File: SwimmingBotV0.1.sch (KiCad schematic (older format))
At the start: 15 parts, among them P1 DCMI, P2 ANALOG

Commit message: woohoo getting there
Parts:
- removed W3: GND, Measurement_Points:Measurement_Point_Round-SMD-Pad_Small, symbol TEST_1P
- removed W6: VBAT, Measurement_Points:Measurement_Point_Round-SMD-Pad_Small, symbol TEST_1P
- removed W7: AUX_3.3V, Measurement_Points:Measurement_Point_Round-SMD-Pad_Small, symbol TEST_1P
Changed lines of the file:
@@
 Text Label 7650 1800 2    60   ~ 0
 MOT2_CS#
-Text Label 4400 6200 2    60   ~ 0
+Text Label 4400 6900 2    60   ~ 0
 MOT2_CS#
-Text Label 4400 6100 2    60   ~ 0
+Text Label 4400 7100 2    60   ~ 0
 MOT1_CS#
-Text Label 6550 5850 0    60   ~ 0
+Text Label 4400 7400 2    60   ~ 0
 RF_CRESP#
 Text Label 9900 1800 2    60   ~ 0
@@
 Text Label 9900 1650 2    60   ~ 0
 RF_CRESP#
-Text Label 6550 5950 0    60   ~ 0
+Text Label 4400 7500 2    60   ~ 0
 RF_EX
-Text Label 6550 6050 0    60   ~ 0
+Text Label 6550 6500 0    60   ~ 0
 RF_CMD#
-Text Label 6550 6150 0    60   ~ 0
+Text Label 6550 6600 0    60   ~ 0
 RF_PWR_DWN#
 Text Label 9450 4950 2    60   ~ 0
@@
 Text Label 6550 6350 0    60   ~ 0
 GYRO_FSYNC
-Text Label 6550 6250 0    60   ~ 0
+Text Label 4400 6100 2    60   ~ 0
 GYRO_INT
 Text Label 7650 1400 2    60   ~ 0
@@
 Text Label 3600 1000 0    60   ~ 0
 3.3V_EN
-Text Label 4400 6850 2    60   ~ 0
+Text Label 6550 6800 0    60   ~ 0
 3.3V_EN
 NoConn ~ 4400 5700
@@
 Text Label 7650 2100 2    60   ~ 0
 MOT2_RST#
-Text Label 4400 6300 2    60   ~ 0
+Text Label 6550 5850 0    60   ~ 0
 MOT1_RST#
-Text Label 4400 6400 2    60   ~ 0
+Text Label 6550 6050 0    60   ~ 0
 MOT2_RST#
 Text Label 2700 3300 0    60   ~ 0
@@
 Text Label 1750 2200 0    60   ~ 0
 CHG_EN#
-Text Label 4400 7000 2    60   ~ 0
+Text Label 4400 7300 2    60   ~ 0
 CHG_STAT1
-Text Label 4400 7100 2    60   ~ 0
+Text Label 6550 6700 0    60   ~ 0
 CHG_STAT2
+Text Label 6550 6150 0    60   ~ 0
+CHG_TE#
 Text Label 4400 7200 2    60   ~ 0
-CHG_TE#
-Text Label 4400 7300 2    60   ~ 0
 CHG_EN#
 Text Label 9450 5350 2    60   ~ 0
@@
 Text Label 9450 5650 2    60   ~ 0
 SD_DETECT
-Text Label 6550 6500 0    60   ~ 0
+Text Label 4400 6400 2    60   ~ 0
 SD_CD
-Text Label 6550 6600 0    60   ~ 0
+Text Label 4400 6500 2    60   ~ 0
 SD_DETECT
 Text Label 1750 1100 0    60   ~ 0
 2S_EN
-Text Label 4400 7400 2    60   ~ 0
+Text Label 6550 6250 0    60   ~ 0
 2S_EN
 $Sheet
@@
 F101 "PC10" I R 6550 6150 60
 F102 "PC12" I R 6550 6250 60
-F103 "PD3" I L 4400 6850 60
-F104 "PG11" I R 6550 6700 60
-F105 "PG12" I R 6550 6800 60
-F106 "PG13" I R 6550 6900 60
-F107 "PG14" I R 6550 7000 60
-F108 "PB7" I L 4400 7100 60
-F109 "PB0" I L 4400 7000 60
-F110 "A0" I R 6550 7150 60
-F111 "A1" I R 6550 7250 60
-F112 "A2" I R 6550 7350 60
-F113 "A3" I R 6550 7450 60
+F103 "PG11" I R 6550 6700 60
+F104 "PG12" I R 6550 6800 60
+F105 "PG13" I R 6550 6900 60
+F106 "PG14" I R 6550 7000 60
+F107 "PB0" I L 4400 6900 60
+F108 "A0" I R 6550 7150 60
+F109 "A1" I R 6550 7250 60
+F110 "A2" I R 6550 7350 60
+F111 "A3" I R 6550 7450 60
+F112 "PB11" I L 4400 7000 60
+F113 "PB10" I L 4400 7100 60
 $EndSheet
 $Comp
@@
 Text Label 7100 1250 0    60   ~ 0
 GND
-Text Label 6550 6700 0    60   ~ 0
+Text Label 4400 6200 2    60   ~ 0
 EXT1
-Text Label 6550 6800 0    60   ~ 0
+Text Label 4400 6300 2    60   ~ 0
 EXT2
 Text Label 7450 5150 2    60   ~ 0
@@
 Text Label 7750 5150 2    60   ~ 0
 EXT2
-Text Label 8300 6050 0    60   ~ 0
-GEN_3.3V
 Text Label 8850 1400 0    60   ~ 0
 MOT1_DIAG
 Text Label 8850 1500 0    60   ~ 0
 MOT2_DIAG
-Text Label 4400 6500 2    60   ~ 0
+Text Label 4400 7000 2    60   ~ 0
 MOT1_DIAG
-Text Label 4400 7500 2    60   ~ 0
+Text Label 6550 5950 0    60   ~ 0
 MOT2_DIAG
 Text Label 1750 1700 0    60   ~ 0
@@
 Text Label 6550 7000 0    60   ~ 0
 5V_CHG
-Text Label 8300 5750 0    60   ~ 0
-VBAT
 Text Label 8300 5400 0    60   ~ 0
 SDA
@@
 $EndComp
 $Comp
-L TEST_1P W6
-U 1 1 575A4CA1
-P 8300 5750
-F 0 "W6" H 8300 6020 50  0000 C CNN
-F 1 "VBAT" H 8300 5950 50  0000 C CNN
-F 2 "Measurement_Points:Measurement_Point_Round-SMD-Pad_Small" H 8500 5750 50  0001 C CNN
-F 3 "" H 8500 5750 50  0000 C CNN
-	1    8300 5750
-	0    -1   -1   0
-$EndComp
-$Comp
-L TEST_1P W7
-U 1 1 575A520C
-P 8300 6050
-F 0 "W7" H 8300 6320 50  0000 C CNN
-F 1 "AUX_3.3V" H 8300 6250 50  0000 C CNN
-F 2 "Measurement_Points:Measurement_Point_Round-SMD-Pad_Small" H 8500 6050 50  0001 C CNN
-F 3 "" H 8500 6050 50  0000 C CNN
-	1    8300 6050
-	0    -1   -1   0
-$EndComp
-$Comp
 L LED D4
 U 1 1 575B30FD
@@
 Wire Wire Line
 	7750 4850 7750 4800
-Text Label 8300 6350 0    60   ~ 0
-GND
 Wire Wire Line
 	6600 7250 6550 7250
@@
 Text Label 2600 1050 2    60   ~ 0
 GEN_3.3V
-$Comp
-L TEST_1P W3
-U 1 1 57400D21
-P 8300 6350
-F 0 "W3" H 8300 6620 50  0000 C CNN
-F 1 "GND" H 8300 6550 50  0000 C CNN
-F 2 "Measurement_Points:Measurement_Point_Round-SMD-Pad_Small" H 8500 6350 50  0001 C CNN
-F 3 "" H 8500 6350 50  0000 C CNN
-	1    8300 6350
-	0    -1   -1   0
-$EndComp
 Text Label 6600 7550 0    60   ~ 0
 GND

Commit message: not final, moving towards board v0.2
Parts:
- R19: value 10k -> 4.1k-3.9k
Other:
- note added: "Note: PC13 is limited to an \ninput or v. weak output"
- note added: "gives 2.5v (vref) when\nvbat is 8.6 or so"
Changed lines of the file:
@@
 P 7700 3950
 F 0 "R19" V 7780 3950 50  0000 C CNN
-F 1 "10k" V 7700 3950 50  0000 C CNN
+F 1 "4.1k-3.9k" V 7700 3950 50  0000 C CNN
 F 2 "Resistors_SMD:R_0402" V 7630 3950 50  0001 C CNN
 F 3 "" H 7700 3950 50  0000 C CNN
@@
 	0    -1   -1   0
 $EndComp
+Text Notes 7150 6300 0    60   ~ 0
+Note: PC13 is limited to an \ninput or v. weak output
+Text Notes 8000 3900 0    60   ~ 0
+gives 2.5v (vref) when\nvbat is 8.6 or so
 $EndSCHEMATC

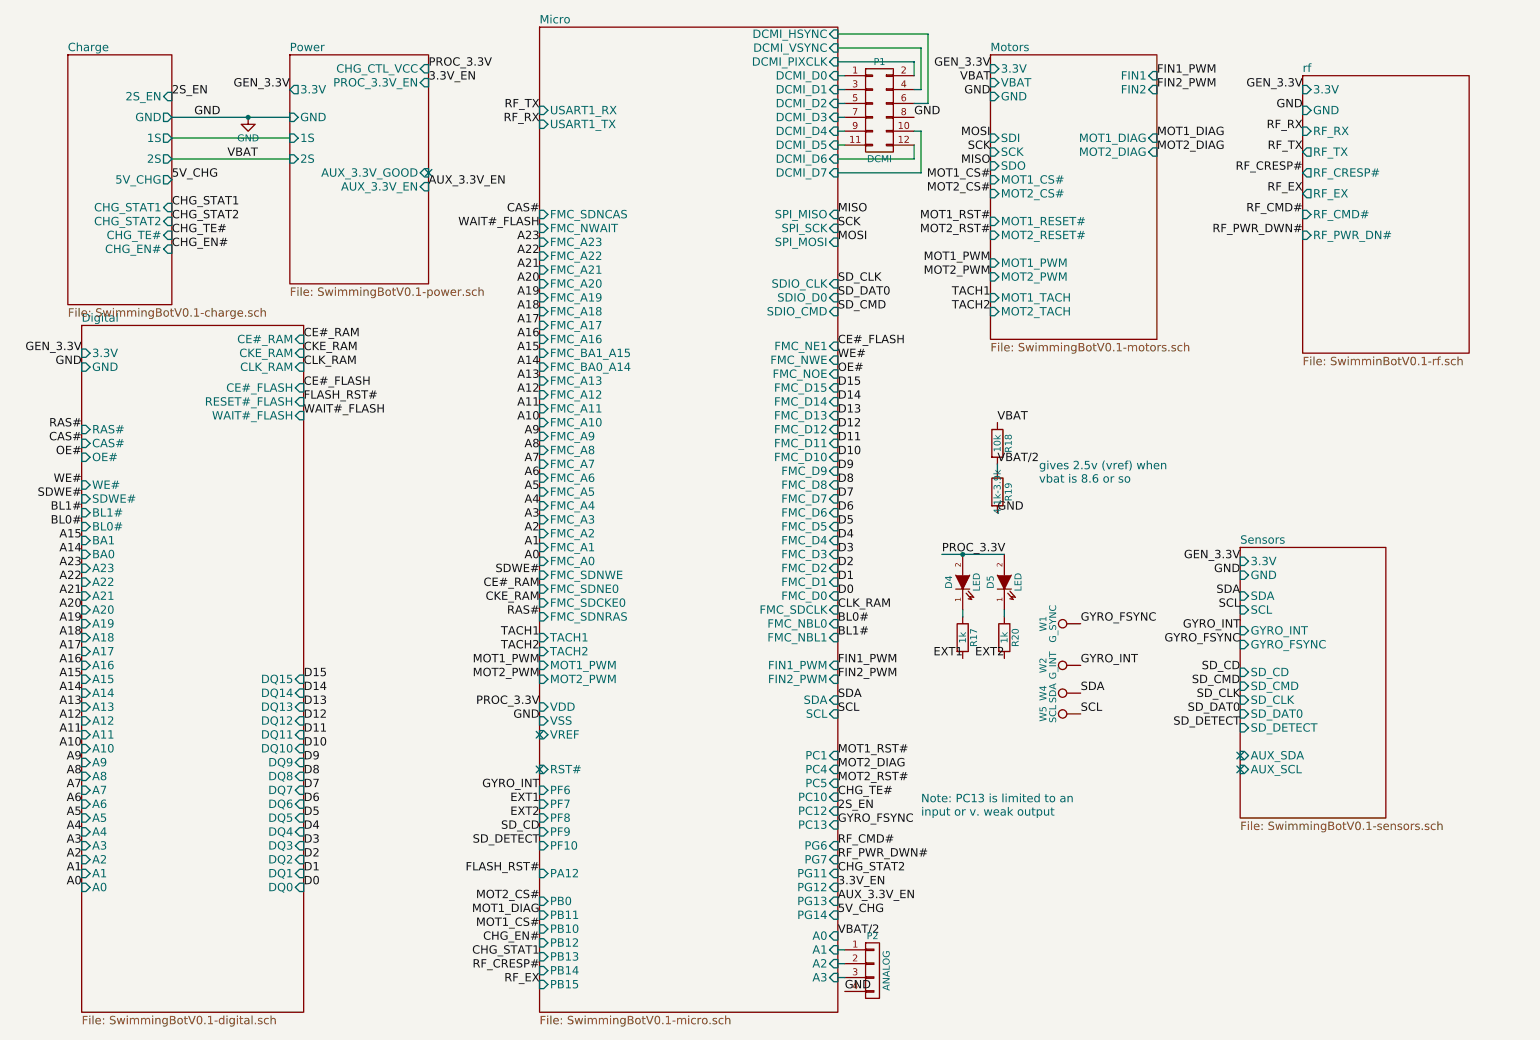
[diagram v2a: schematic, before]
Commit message: removed old ram and flash, added new flash, switched to 100 pin micro
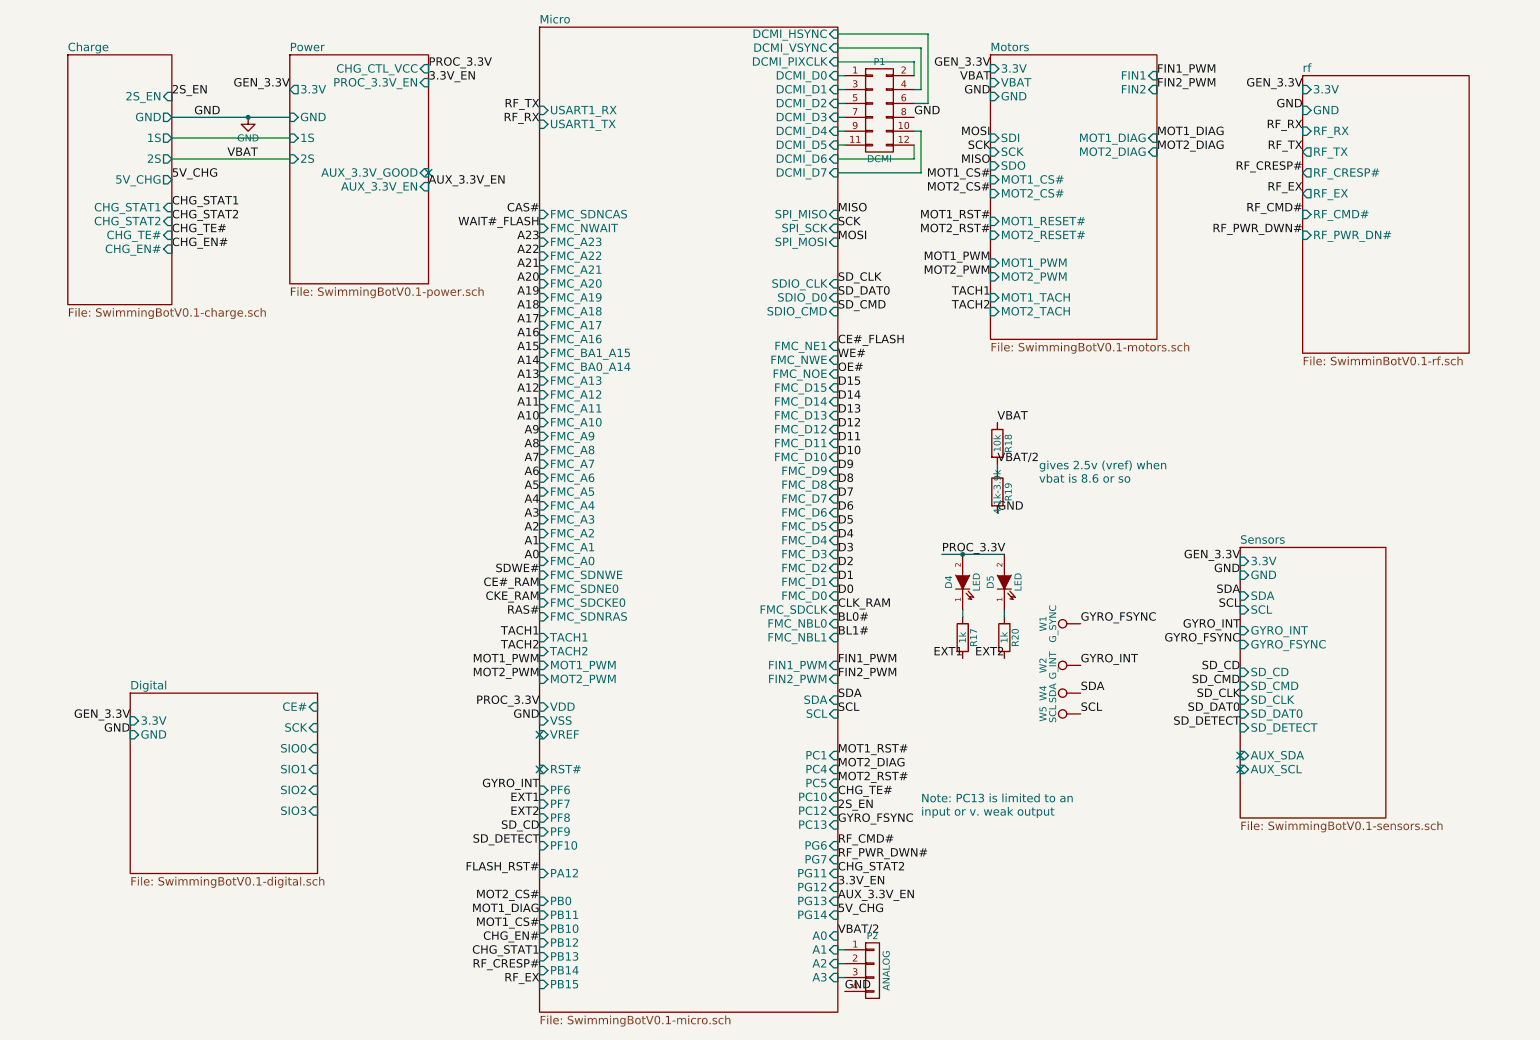
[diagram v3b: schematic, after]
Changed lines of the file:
@@
 Connection ~ 2300 1250
 $Sheet
-S 1100 2750 1600 4950
+S 1450 5400 1350 1300
 U 56D60FDB
 F0 "Digital" 60
 F1 "SwimmingBotV0.1-digital.sch" 60
-F2 "3.3V" I L 1100 2950 60
-F3 "GND" I L 1100 3050 60
-F4 "A0" I L 1100 6800 60
-F5 "A1" I L 1100 6700 60
-F6 "A2" I L 1100 6600 60
-F7 "A3" I L 1100 6500 60
-F8 "A4" I L 1100 6400 60
-F9 "A5" I L 1100 6300 60
-F10 "A6" I L 1100 6200 60
-F11 "A7" I L 1100 6100 60
-F12 "A8" I L 1100 6000 60
-F13 "A9" I L 1100 5900 60
-F14 "A10" I L 1100 5800 60
-F15 "A11" I L 1100 5700 60
-F16 "A12" I L 1100 5600 60
-F17 "A13" I L 1100 5500 60
-F18 "A14" I L 1100 5400 60
-F19 "A15" I L 1100 5300 60
-F20 "A16" I L 1100 5200 60
-F21 "A17" I L 1100 5100 60
-F22 "A18" I L 1100 5000 60
-F23 "A19" I L 1100 4900 60
-F24 "A20" I L 1100 4800 60
-F25 "A21" I L 1100 4700 60
-F26 "A22" I L 1100 4600 60
-F27 "A23" I L 1100 4500 60
-F28 "CE#_FLASH" I R 2700 3200 60
-F29 "WE#" I L 1100 3900 60
-F30 "CE#_RAM" I R 2700 2850 60
-F31 "DQ0" I R 2700 6800 60
-F32 "DQ1" I R 2700 6700 60
-F33 "DQ2" I R 2700 6600 60
-F34 "DQ3" I R 2700 6500 60
-F35 "DQ4" I R 2700 6400 60
-F36 "DQ5" I R 2700 6300 60
-F37 "DQ6" I R 2700 6200 60
-F38 "DQ7" I R 2700 6100 60
-F39 "DQ8" I R 2700 6000 60
-F40 "DQ9" I R 2700 5900 60
-F41 "DQ10" I R 2700 5800 60
-F42 "DQ11" I R 2700 5700 60
-F43 "DQ12" I R 2700 5600 60
-F44 "DQ13" I R 2700 5500 60
-F45 "DQ14" I R 2700 5400 60
-F46 "DQ15" I R 2700 5300 60
-F47 "OE#" I L 1100 3700 60
-F48 "CAS#" I L 1100 3600 60
-F49 "RAS#" I L 1100 3500 60
-F50 "CLK_RAM" I R 2700 3050 60
-F51 "CKE_RAM" I R 2700 2950 60
-F52 "RESET#_FLASH" I R 2700 3300 60
-F53 "WAIT#_FLASH" I R 2700 3400 60
-F54 "BL1#" I L 1100 4100 60
-F55 "BL0#" I L 1100 4200 60
-F56 "BA0" I L 1100 4400 60
-F57 "BA1" I L 1100 4300 60
-F58 "SDWE#" I L 1100 4000 60
+F2 "3.3V" I L 1450 5600 60
+F3 "GND" I L 1450 5700 60
+F4 "CE#" I R 2800 5500 60
+F5 "SIO1" I R 2800 5950 60
+F6 "SIO2" I R 2800 6100 60
+F7 "SIO3" I R 2800 6250 60
+F8 "SCK" I R 2800 5650 60
+F9 "SIO0" I R 2800 5800 60
 $EndSheet
 $Sheet
@@
 Text Label 4400 2250 2    60   ~ 0
 A22
-Text Label 1100 6800 2    60   ~ 0
-A0
-Text Label 1100 6700 2    60   ~ 0
-A1
-Text Label 1100 6600 2    60   ~ 0
-A2
-Text Label 1100 6500 2    60   ~ 0
-A3
-Text Label 1100 6400 2    60   ~ 0
-A4
-Text Label 1100 6300 2    60   ~ 0
-A5
-Text Label 1100 6200 2    60   ~ 0
-A6
-Text Label 1100 6100 2    60   ~ 0
-A7
-Text Label 1100 6000 2    60   ~ 0
-A8
-Text Label 1100 5900 2    60   ~ 0
-A9
-Text Label 1100 5800 2    60   ~ 0
-A10
-Text Label 1100 5700 2    60   ~ 0
-A11
-Text Label 1100 5600 2    60   ~ 0
-A12
-Text Label 1100 5500 2    60   ~ 0
-A13
-Text Label 1100 5400 2    60   ~ 0
-A14
-Text Label 1100 5300 2    60   ~ 0
-A15
-Text Label 1100 5200 2    60   ~ 0
-A16
-Text Label 1100 5100 2    60   ~ 0
-A17
-Text Label 1100 5000 2    60   ~ 0
-A18
-Text Label 1100 4900 2    60   ~ 0
-A19
-Text Label 1100 4800 2    60   ~ 0
-A20
-Text Label 1100 4700 2    60   ~ 0
-A21
-Text Label 1100 4600 2    60   ~ 0
-A22
-Text Label 1100 4500 2    60   ~ 0
-A23
 Text Label 4400 2150 2    60   ~ 0
 A23
-Text Label 1100 4300 2    60   ~ 0
-A15
-Text Label 1100 4400 2    60   ~ 0
-A14
-Text Label 2700 6800 0    60   ~ 0
-D0
-Text Label 2700 6700 0    60   ~ 0
-D1
-Text Label 2700 6600 0    60   ~ 0
-D2
-Text Label 2700 6500 0    60   ~ 0
-D3
-Text Label 2700 6400 0    60   ~ 0
-D4
-Text Label 2700 6300 0    60   ~ 0
-D5
-Text Label 2700 6200 0    60   ~ 0
-D6
-Text Label 2700 6100 0    60   ~ 0
-D7
-Text Label 2700 6000 0    60   ~ 0
-D8
-Text Label 2700 5900 0    60   ~ 0
-D9
-Text Label 2700 5800 0    60   ~ 0
-D10
-Text Label 2700 5700 0    60   ~ 0
-D11
-Text Label 2700 5600 0    60   ~ 0
-D12
-Text Label 2700 5500 0    60   ~ 0
-D13
-Text Label 2700 5400 0    60   ~ 0
-D14
-Text Label 2700 5300 0    60   ~ 0
-D15
 Text Label 6550 4700 0    60   ~ 0
 D0
@@
 Text Label 6550 3200 0    60   ~ 0
 D15
-Text Label 2700 2850 0    60   ~ 0
-CE#_RAM
 Text Label 4400 4650 2    60   ~ 0
 CE#_RAM
-Text Label 2700 2950 0    60   ~ 0
-CKE_RAM
 Text Label 4400 4750 2    60   ~ 0
 CKE_RAM
-Text Label 1100 3500 2    60   ~ 0
-RAS#
 Text Label 4400 4850 2    60   ~ 0
 RAS#
 Text Label 6550 4800 0    60   ~ 0
 CLK_RAM
-Text Label 2700 3050 0    60   ~ 0
-CLK_RAM
 Text Label 6550 2900 0    60   ~ 0
 CE#_FLASH
-Text Label 2700 3200 0    60   ~ 0
-CE#_FLASH
-Text Label 2700 3400 0    60   ~ 0
-WAIT#_FLASH
 Text Label 4400 2050 2    60   ~ 0
 WAIT#_FLASH
 Text Label 4400 1950 2    60   ~ 0
 CAS#
-Text Label 1100 3600 2    60   ~ 0
-CAS#
-Text Label 1100 4000 2    60   ~ 0
-SDWE#
-Text Label 1100 3700 2    60   ~ 0
-OE#
-Text Label 1100 3900 2    60   ~ 0
-WE#
 Text Label 6550 3100 0    60   ~ 0
 OE#
@@
 Text Label 6550 5000 0    60   ~ 0
 BL1#
-Text Label 1100 4100 2    60   ~ 0
-BL1#
-Text Label 1100 4200 2    60   ~ 0
-BL0#
 Text Label 9900 1350 2    60   ~ 0
 RF_RX
@@
 Text Label 9450 4550 2    60   ~ 0
 GND
-Text Label 1100 3050 2    60   ~ 0
+Text Label 1450 5700 2    60   ~ 0
 GND
 Text Label 3600 900  0    60   ~ 0
@@
 Text Label 9450 4450 2    60   ~ 0
 GEN_3.3V
-Text Label 1100 2950 2    60   ~ 0
+Text Label 1450 5600 2    60   ~ 0
 GEN_3.3V
 Text Label 7650 1700 2    60   ~ 0
@@
 Text Label 6550 6050 0    60   ~ 0
 MOT2_RST#
-Text Label 2700 3300 0    60   ~ 0
-FLASH_RST#
 Text Label 4400 6700 2    60   ~ 0
 FLASH_RST#
@@
 $EndComp
 Wire Wire Line
-	7300 4400 7750 4400
+	7300 4400 7450 4400
+Wire Wire Line
+	7450 4400 7750 4400
 Connection ~ 7450 4400
 Text Label 7300 4400 0    60   ~ 0
@@
 	1750 1550 2600 1550
 Wire Wire Line
-	1750 1250 2600 1250
+	1750 1250 2300 1250
+Wire Wire Line
+	2300 1250 2600 1250
 $Sheet
 S 1000 800  750  1800

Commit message: swapped out battery serializing hardware from discrete to IC, and standard level fets
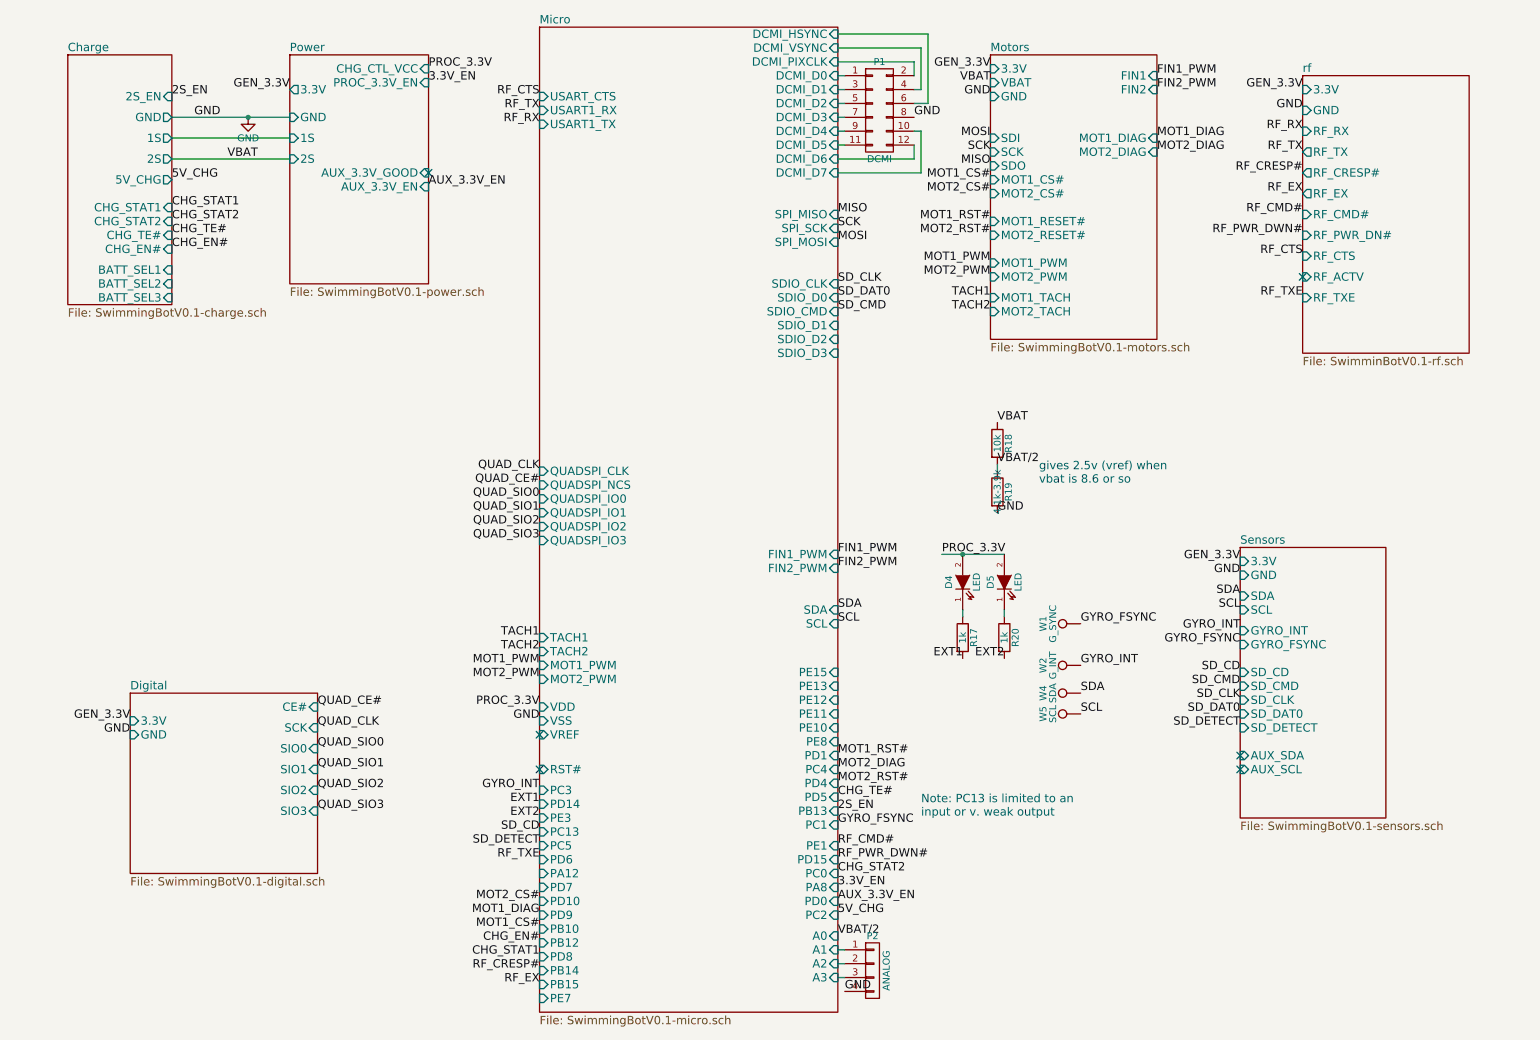
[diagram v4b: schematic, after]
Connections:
- no-connect marks 5 -> 6
